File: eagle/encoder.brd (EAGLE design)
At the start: 100 x 80 mm, 27 parts, among them IC1 LM339D, J1 SPI, U1 MCP42XXX, U2 ATMEGA328P

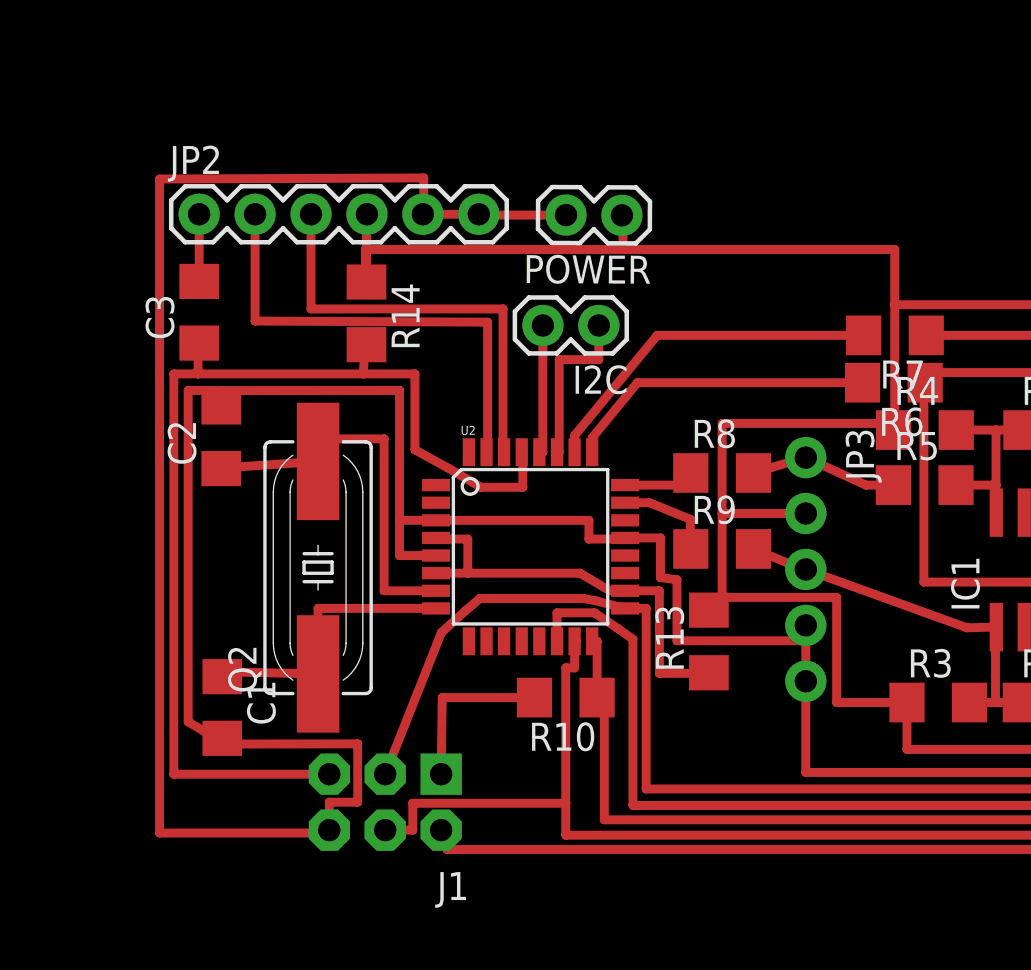
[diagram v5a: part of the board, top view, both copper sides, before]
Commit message: Fixed an issue where the digital output channels were not connected to interrupts.
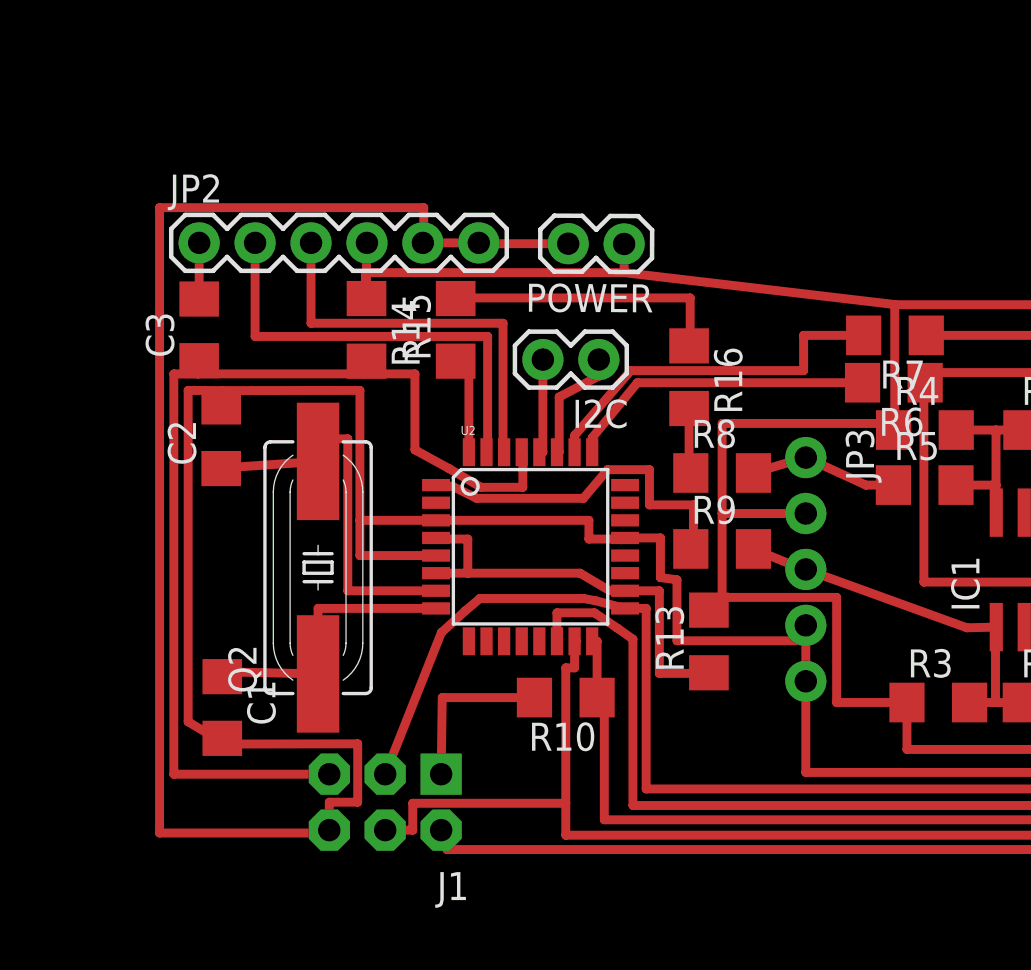
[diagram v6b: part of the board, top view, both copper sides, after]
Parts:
- added R15, R16: 0, resistor:R1206
- moved I2C 1.55 mm to (54.7, 58.8)
- moved POWER 1.30 mm to (55.9, 64.0)
- moved JP2 1.30 mm to (36.5, 64.0)
- moved C3 0.80 mm to (36.5, 60.1)
- moved R14 0.75 mm to (44.1, 60.1)
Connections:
- new net N$14: R15.2, R16.1
- new net N$15: R16.2, R8.1
- net N$6: now also R15.1, U2.32; no longer R8.1, U2.24
- net N$7: now also U2.1; no longer U2.23
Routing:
- net N$14: track 0.00 -> 12.9 mm
- net N$7: track 4.45 -> 16.2 mm
- net +5V: track 214.3 -> 210.7 mm
- net N$15: track 0.00 -> 3.01 mm
- net N$12: track 7.66 -> 5.39 mm
- net RESET: track 49.5 -> 47.9 mm
- net N$13: track 5.92 -> 4.37 mm
- net RX-I: track 19.6 -> 18.3 mm
- net TX-O: track 21.4 -> 20.1 mm
- net N$6: track 3.54 -> 4.74 mm
- net A-ANALOG-IN: track 16.0 -> 16.8 mm
- net GND: track 194.5 -> 195.0 mm
- net DTR: track 3.05 -> 2.55 mm

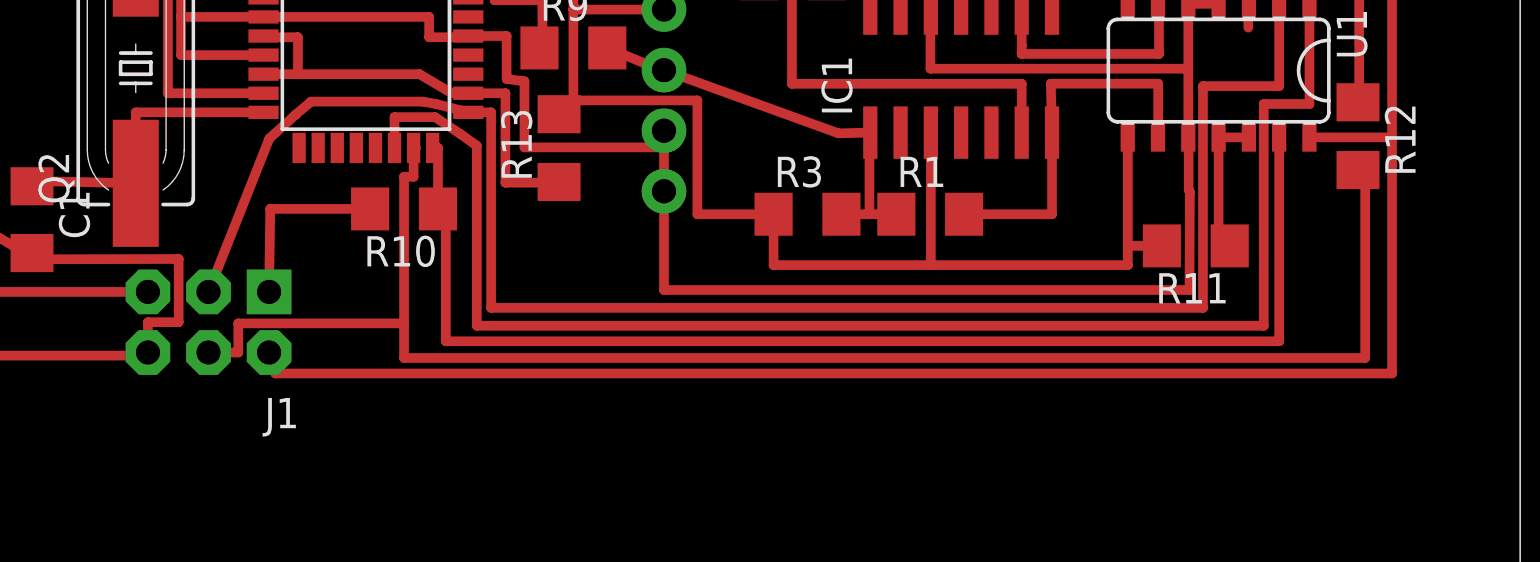
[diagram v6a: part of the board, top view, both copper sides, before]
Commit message: Added LED indicator.
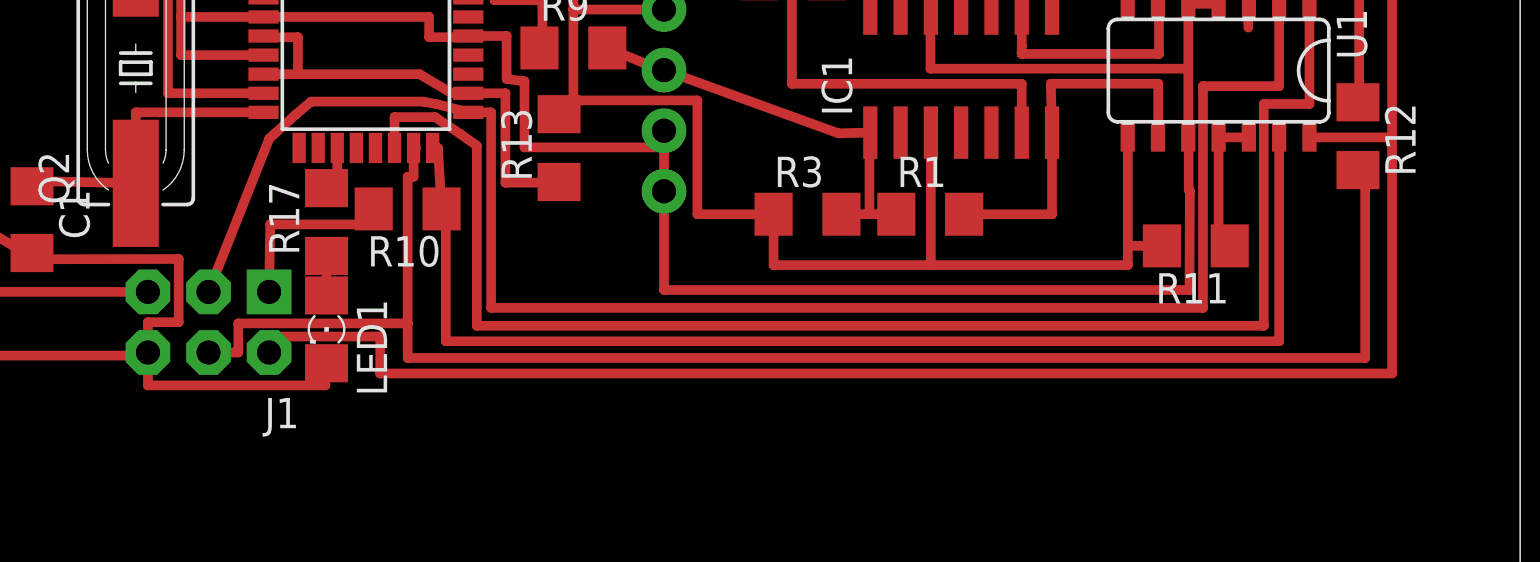
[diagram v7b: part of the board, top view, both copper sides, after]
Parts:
- added LED1: (no value), led:1206
- added R17: 330, resistor:R1206
- moved R10 0.15 mm to (53.4, 43.4)
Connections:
- new net N$16: LED1.A, R17.1
- new net N$17: R17.2, U2.11
- net GND: now also LED1.C
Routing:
- net GND: track 195.0 -> 204.8 mm
- net N$17: track 0.00 -> 2.14 mm
- net N$16: track 0.00 -> 1.66 mm
- net +5V: track 210.7 -> 212.0 mm
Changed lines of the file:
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@@
 <element name="R8" library="resistor" package="R1206" value="0" x="60.3" y="53.6"/>
 <element name="R9" library="resistor" package="R1206" value="0" x="60.3" y="50.15"/>
-<element name="R10" library="resistor" package="R1206" value="0" x="53.2" y="43.4" rot="R180"/>
+<element name="R10" library="resistor" package="R1206" value="0" x="53.35" y="43.4" rot="R180"/>
 <element name="J1" library="SparkFun-Connectors" package="2X3-NS" value="SPI" x="45" y="38.65" rot="R180"/>
 <element name="R11" library="resistor" package="R1206" value="0" x="86.4" y="41.85" rot="R180"/>
@@
 <element name="R15" library="resistor" package="R1206" value="0" x="48.2" y="60.1" rot="R90"/>
 <element name="R16" library="resistor" package="R1206" value="0" x="58.8" y="57.95" rot="R270"/>
+<element name="LED1" library="led" package="1206" value="" x="49.95" y="38.35" rot="R270"/>
+<element name="R17" library="resistor" package="R1206" value="330" x="49.95" y="42.85" rot="R90"/>
 </elements>
 <signals>
@@
 <wire x1="64.1" y1="44.14" x2="64.1" y2="40" width="0.4064" layer="1"/>
 <wire x1="64.1" y1="40" x2="86.135" y2="40" width="0.4064" layer="1"/>
-<wire x1="86.135" y1="40" x2="86.15" y2="44.1" width="0.4064" layer="1"/>
-<wire x1="86.15" y1="44.1" x2="86.1" y2="44.2" width="0.4064" layer="1"/>
+<wire x1="86.135" y1="40" x2="86.15" y2="44.15" width="0.4064" layer="1"/>
+<wire x1="86.15" y1="44.15" x2="86.1" y2="44.2" width="0.4064" layer="1"/>
 <wire x1="86.1" y1="44.2" x2="86.1" y2="46.4" width="0.4064" layer="1"/>
 <wire x1="86.1" y1="46.4" x2="86.085" y2="46.4" width="0.4064" layer="1"/>
@@
 <wire x1="53.310034375" y1="64.013296875" x2="49.25" y2="64.013296875" width="0.4064" layer="1"/>
 <wire x1="49.25" y1="64.013296875" x2="49.25" y2="64.05" width="0.4064" layer="1"/>
+<contactref element="LED1" pad="C"/>
+<wire x1="49.95" y1="36.928" x2="49.9" y2="36.928" width="0.4064" layer="1"/>
+<wire x1="49.9" y1="36.928" x2="49.9" y2="36" width="0.4064" layer="1"/>
+<wire x1="49.9" y1="36" x2="42.46" y2="36" width="0.4064" layer="1"/>
+<wire x1="42.46" y1="36" x2="42.46" y2="37.38" width="0.4064" layer="1"/>
 </signal>
 <signal name="N$5">
@@
 <contactref element="J1" pad="2"/>
 <wire x1="47.54" y1="37.38" x2="47.55" y2="37.38" width="0.4064" layer="1"/>
-<wire x1="47.55" y1="37.38" x2="47.8" y2="36.5" width="0.4064" layer="1"/>
-<wire x1="47.8" y1="36.5" x2="94.628775" y2="36.5" width="0.4064" layer="1"/>
+<wire x1="47.55" y1="37.38" x2="47.8" y2="38.05" width="0.4064" layer="1"/>
+<wire x1="47.8" y1="38.05" x2="52.2" y2="38.05" width="0.4064" layer="1"/>
+<wire x1="52.2" y1="38.05" x2="52.2" y2="36.5" width="0.4064" layer="1"/>
+<wire x1="52.2" y1="36.5" x2="94.628775" y2="36.5" width="0.4064" layer="1"/>
 <wire x1="94.628775" y1="36.5" x2="94.628775" y2="46.4" width="0.4064" layer="1"/>
 <contactref element="R11" pad="2"/>
@@
 <contactref element="J1" pad="4"/>
 <wire x1="53.6" y1="45.9574" x2="53.6" y2="44.75" width="0.4064" layer="1"/>
-<wire x1="53.6" y1="44.75" x2="53.2" y2="44.75" width="0.4064" layer="1"/>
-<wire x1="53.2" y1="44.75" x2="53.2" y2="38.6" width="0.4064" layer="1"/>
-<wire x1="53.2" y1="38.6" x2="53.2" y2="37.15" width="0.4064" layer="1"/>
-<wire x1="53.2" y1="37.15" x2="93.5" y2="37.15" width="0.4064" layer="1"/>
+<wire x1="53.6" y1="44.75" x2="53.35" y2="44.75" width="0.4064" layer="1"/>
+<wire x1="53.35" y1="44.75" x2="53.35" y2="38.6" width="0.4064" layer="1"/>
+<wire x1="53.35" y1="38.6" x2="53.35" y2="37.15" width="0.4064" layer="1"/>
+<wire x1="53.35" y1="37.15" x2="93.5" y2="37.15" width="0.4064" layer="1"/>
 <wire x1="45" y1="37.38" x2="46.25" y2="37.38" width="0.4064" layer="1"/>
 <wire x1="46.25" y1="37.38" x2="46.25" y2="38.6" width="0.4064" layer="1"/>
-<wire x1="46.25" y1="38.6" x2="53.2" y2="38.6" width="0.4064" layer="1"/>
+<wire x1="46.25" y1="38.6" x2="53.35" y2="38.6" width="0.4064" layer="1"/>
 <contactref element="R12" pad="2"/>
 <wire x1="93.2" y1="45.028" x2="93.5" y2="45.028" width="0.4064" layer="1"/>
@@
 <contactref element="R10" pad="1"/>
 <wire x1="54.4" y1="45.9574" x2="54.622" y2="45.9574" width="0.4064" layer="1"/>
-<wire x1="54.622" y1="45.9574" x2="54.622" y2="43.4" width="0.4064" layer="1"/>
-<wire x1="54.622" y1="43.4" x2="54.95" y2="43.4" width="0.4064" layer="1"/>
+<wire x1="54.622" y1="45.9574" x2="54.772" y2="43.4" width="0.4064" layer="1"/>
+<wire x1="54.772" y1="43.4" x2="54.95" y2="43.4" width="0.4064" layer="1"/>
 <wire x1="54.95" y1="43.4" x2="54.95" y2="37.85" width="0.4064" layer="1"/>
 <wire x1="54.95" y1="37.85" x2="89.895" y2="37.85" width="0.4064" layer="1"/>
@@
 <contactref element="J1" pad="1"/>
 <contactref element="R10" pad="2"/>
-<wire x1="51.778" y1="43.4" x2="47.59" y2="43.4" width="0.4064" layer="1"/>
-<wire x1="47.59" y1="43.4" x2="47.54" y2="39.92" width="0.4064" layer="1"/>
+<wire x1="51.928" y1="43.4" x2="51.4" y2="43.4" width="0.4064" layer="1"/>
+<wire x1="51.4" y1="43.4" x2="51.4" y2="42.75" width="0.4064" layer="1"/>
+<wire x1="51.4" y1="42.75" x2="47.59" y2="42.75" width="0.4064" layer="1"/>
+<wire x1="47.59" y1="42.75" x2="47.54" y2="39.92" width="0.4064" layer="1"/>
 </signal>
 <signal name="N$4">
@@
 <wire x1="58.8" y1="53.6" x2="58.8" y2="56.528" width="0.4064" layer="1"/>
 </signal>
+<signal name="N$16">
+<contactref element="LED1" pad="A"/>
+<contactref element="R17" pad="1"/>
+<wire x1="49.95" y1="39.772" x2="49.95" y2="41.428" width="0.4064" layer="1"/>
+</signal>
+<signal name="N$17">
+<contactref element="U2" pad="11"/>
+<contactref element="R17" pad="2"/>
+<wire x1="49.95" y1="44.272" x2="50.4" y2="44.272" width="0.4064" layer="1"/>
+<wire x1="50.4" y1="44.272" x2="50.4" y2="45.9574" width="0.4064" layer="1"/>
+</signal>
 </signals>

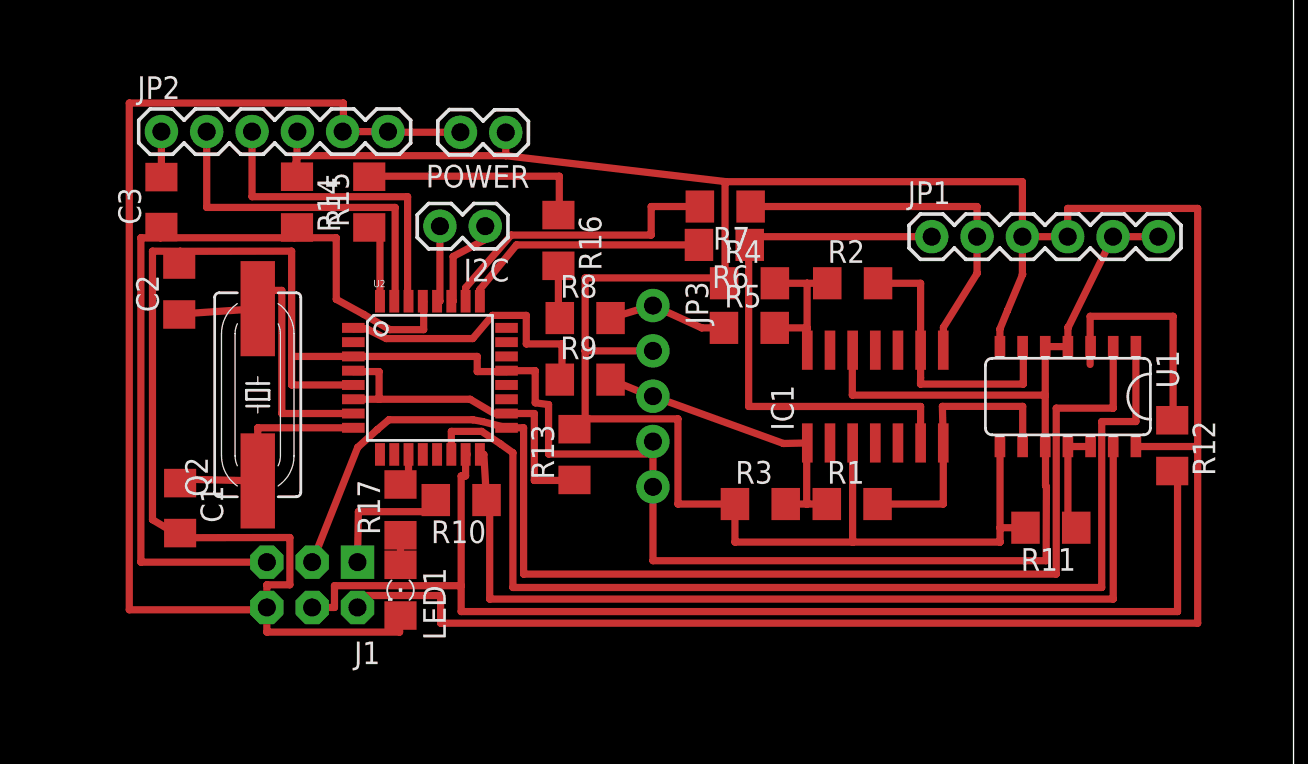
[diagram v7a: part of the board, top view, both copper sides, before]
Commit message: Thinned some traces to provide sufficient clearance.
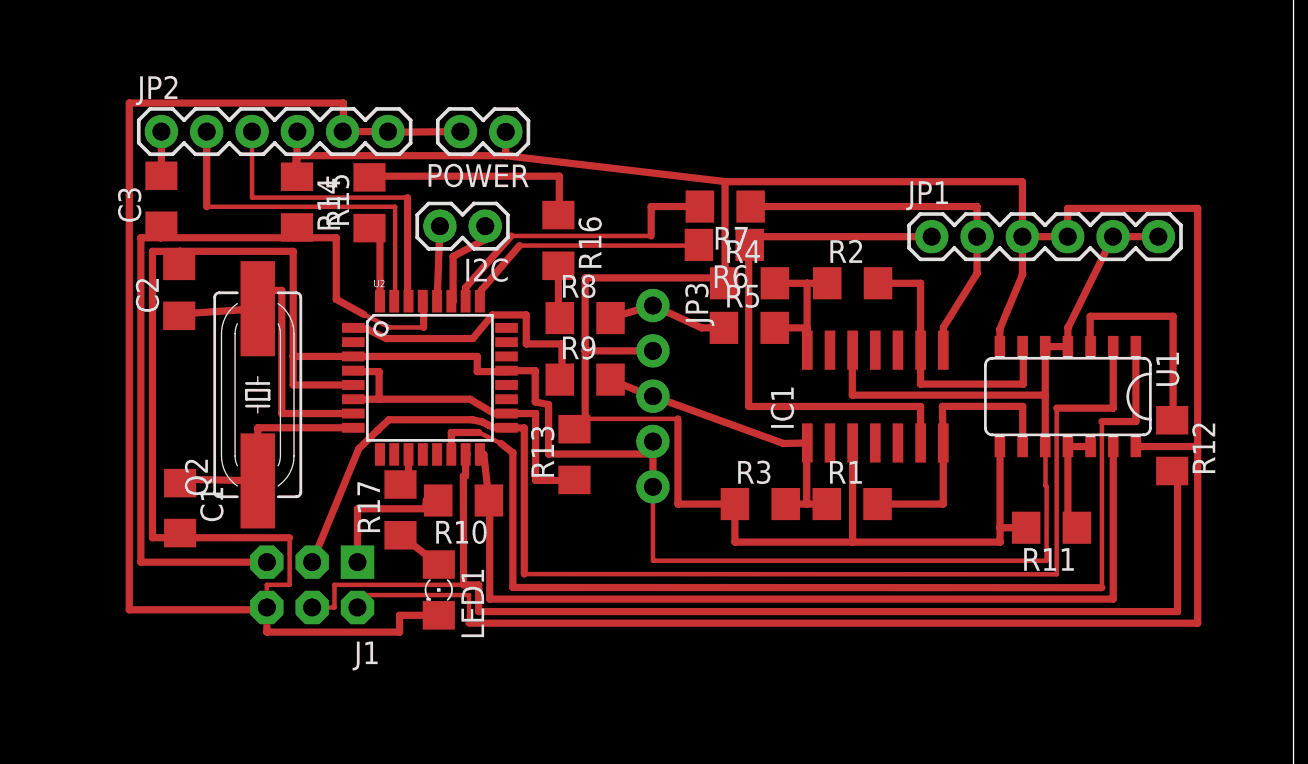
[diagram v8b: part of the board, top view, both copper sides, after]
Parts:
- moved LED1 2.15 mm to (52.1, 38.4)
- moved R10 0.14 mm to (53.5, 43.4)
- moved C2 0.07 mm to (37.5, 55.1)
- moved C3 0.07 mm to (36.5, 60.2)
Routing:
- net GND: track 204.8 -> 207.6 mm
- net N$16: track 1.66 -> 2.70 mm
- net N$8: track 13.2 -> 12.3 mm
